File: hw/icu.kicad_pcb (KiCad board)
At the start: 2 copper layers, 60 x 90 mm, 99 parts, among them J1001 ARM_JTAG_SWD_HEADER_10_PINSMD, J101 AMPSEAL_8_POS_VERT_BLACK_SEAL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, J102 AMPSEAL_23_POS_VERT_GRAY_SEAL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, U1001 MCP2551_SOIC8, U1002 LPC1549JBD64, U301 VND5050AJTR-E, U401 VND5050AJTR-E, U501 VND5050AJTR-E, U601 VND5050AJTR-E, U701 VND5050AJTR-E, U801 VND5050AJTR-E, U901 VND5050AJTR-E, X1001 XTAL_7A-12.000MAAJ-T

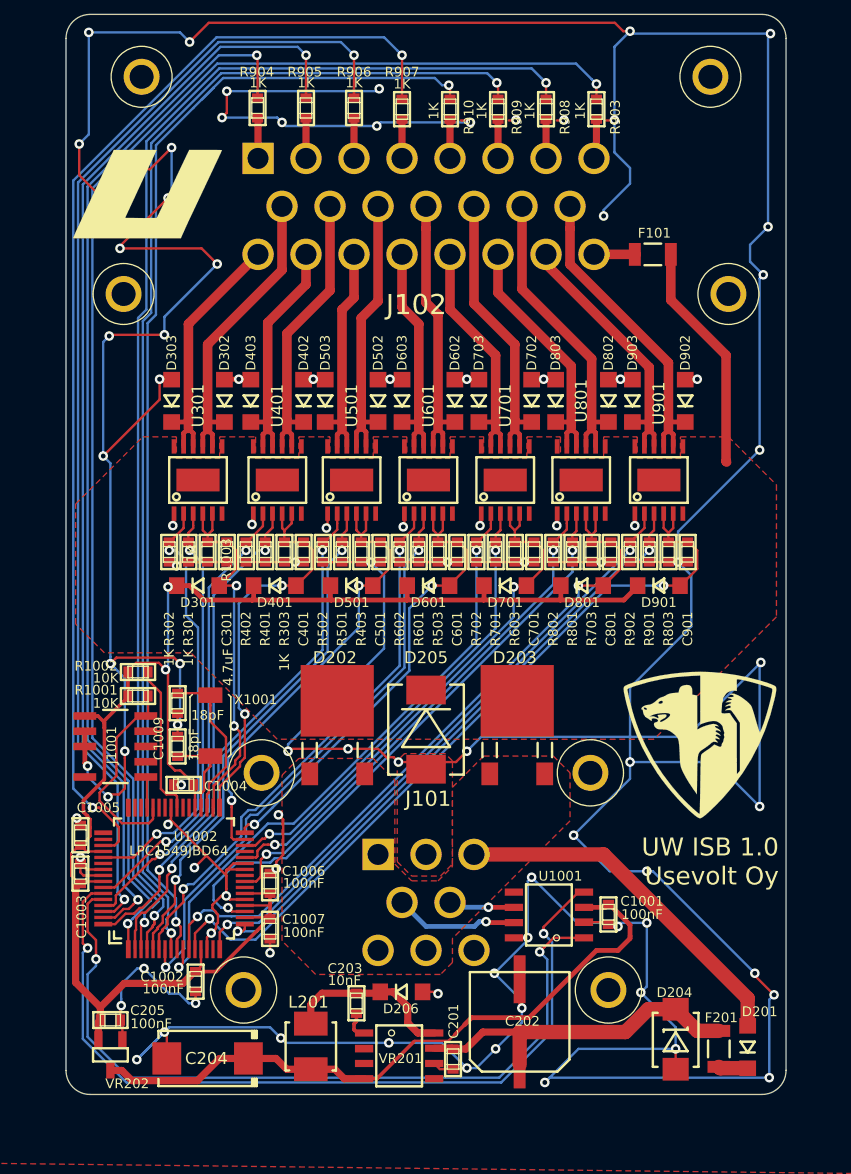
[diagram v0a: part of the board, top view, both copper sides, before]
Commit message: pcb 2.0 created, with imu
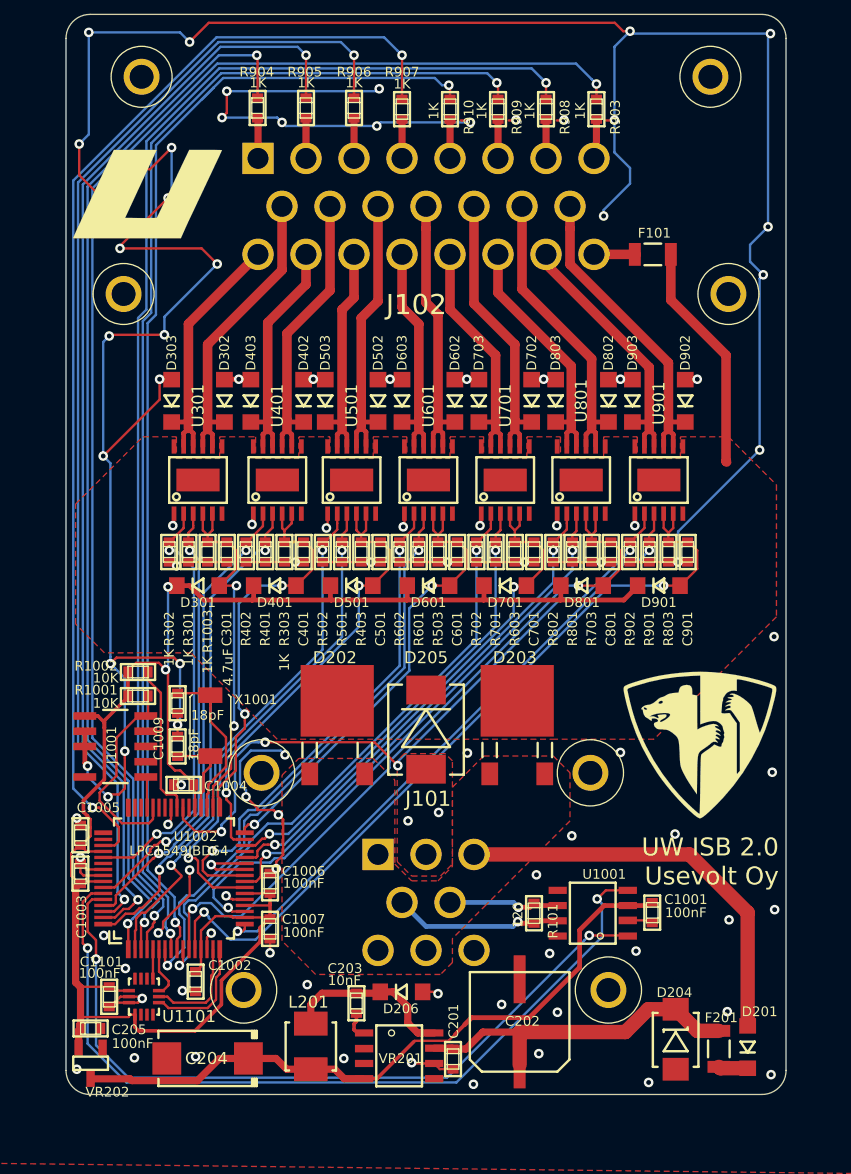
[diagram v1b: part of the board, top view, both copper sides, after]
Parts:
- added C1101: 100nF, kemet:0603, F.Cu at (141.6, 130.9)
- added R101: 120, yageo:0603, F.Cu at (177.0, 123.9)
- added U1101: IMU_LSM6DS3USTR, usevolt:LGA-14, F.Cu at (144.5, 130.9)
- moved C1001 3.65 mm to (186.8, 123.8)
- moved U1001 3.65 mm to (181.9, 123.9)
- moved VR202 1.79 mm to (140.1, 136.4)
- moved C205 1.79 mm to (140.1, 133.5)
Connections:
- net /5V_OUT renamed /VDD_OUT
- U1002 pad P$15: (no net) -> /lpc1549/SCK
- U1002 pad P$16: /Sheet5A7B753C/IN2 -> /Sheet5B43633F/CS
- U1002 pad P$23: (no net) -> /Sheet5A7B341A/IN1
- U1002 pad P$25: (no net) -> /Sheet5A7B3FAC/IN2
- U1002 pad P$39: (no net) -> /Sheet5A7B753C/IN2
- U1002 pad P$5: /Sheet5A7B341A/IN1 -> /Sheet5B43633F/MISO
- U1002 pad P$6: /Sheet5A7B3FAC/IN2 -> /Sheet5B43633F/MOSI
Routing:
- net GND: track 661.3 -> 399.1 mm, vias 96 -> 100
- net +3V3: track 138.6 -> 154.2 mm
- net /Sheet5B43633F/CS: track 0.00 -> 10.2 mm
- net /lpc1549/SCK: track 0.00 -> 8.81 mm
- net /Sheet5B43633F/MOSI: track 0.00 -> 4.32 mm
- net /Sheet5A7B753C/IN2: track 52.4 -> 56.7 mm, vias 2 -> 4
- net /Power supply/VIN: track 30.1 -> 34.2 mm
- net /lpc1549/CANL: track 5.49 -> 9.36 mm
- net /lpc1549/CANH: track 10.3 -> 14.1 mm
- net /Sheet5A7B3FAC/IN2: track 45.7 -> 42.0 mm
- net /Sheet5A7B341A/IN1: track 43.0 -> 40.5 mm
- net /Sheet5B43633F/MISO: track 0.00 -> 2.46 mm
- net /lpc1549/CAN_TX: track 65.4 -> 63.9 mm
- net /lpc1549/OUT7_SENSE: track 65.7 -> 66.8 mm
- net /lpc1549/OUT6_SENSE: track 59.9 -> 60.8 mm
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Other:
- board text added: "UW ISB 2.0 Usevolt Oy"
- board text removed: "UW ISB 1.0 Usevolt Oy"

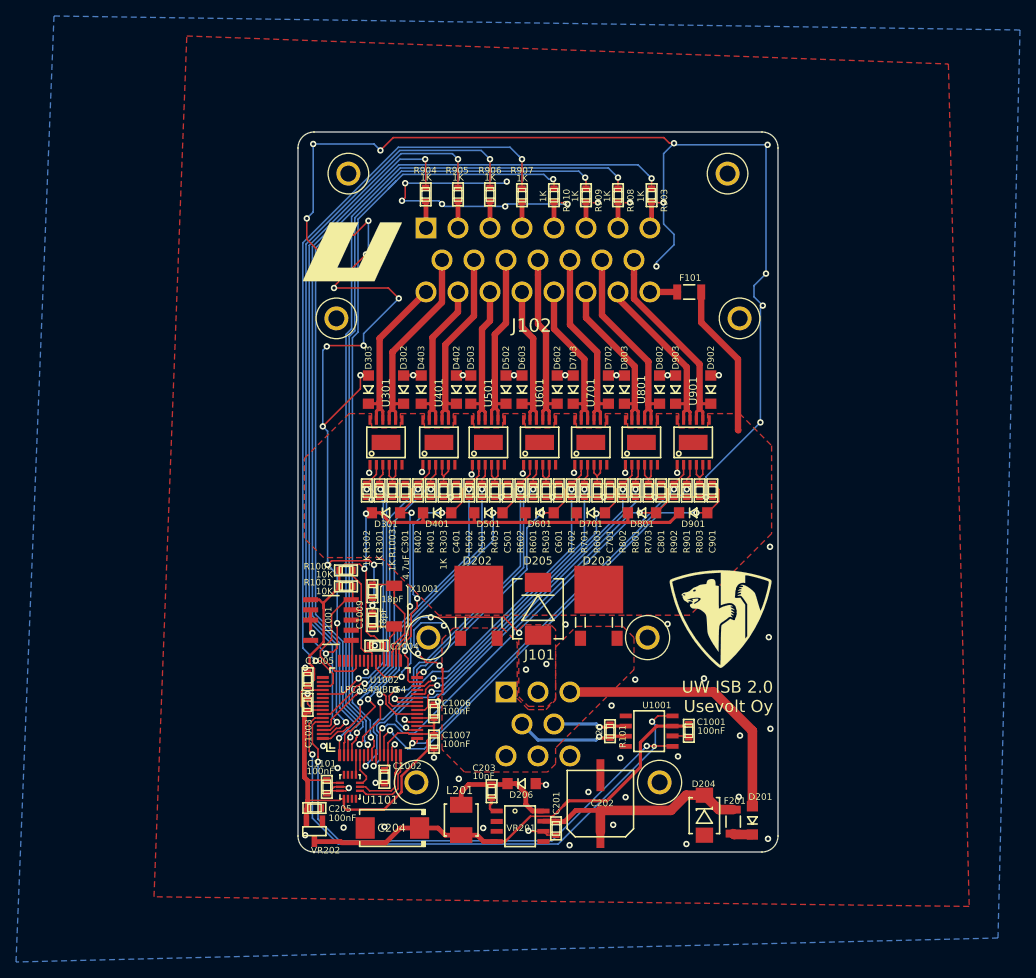
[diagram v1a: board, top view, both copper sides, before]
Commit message: 2 din replaced with ain, zeners added to outputs
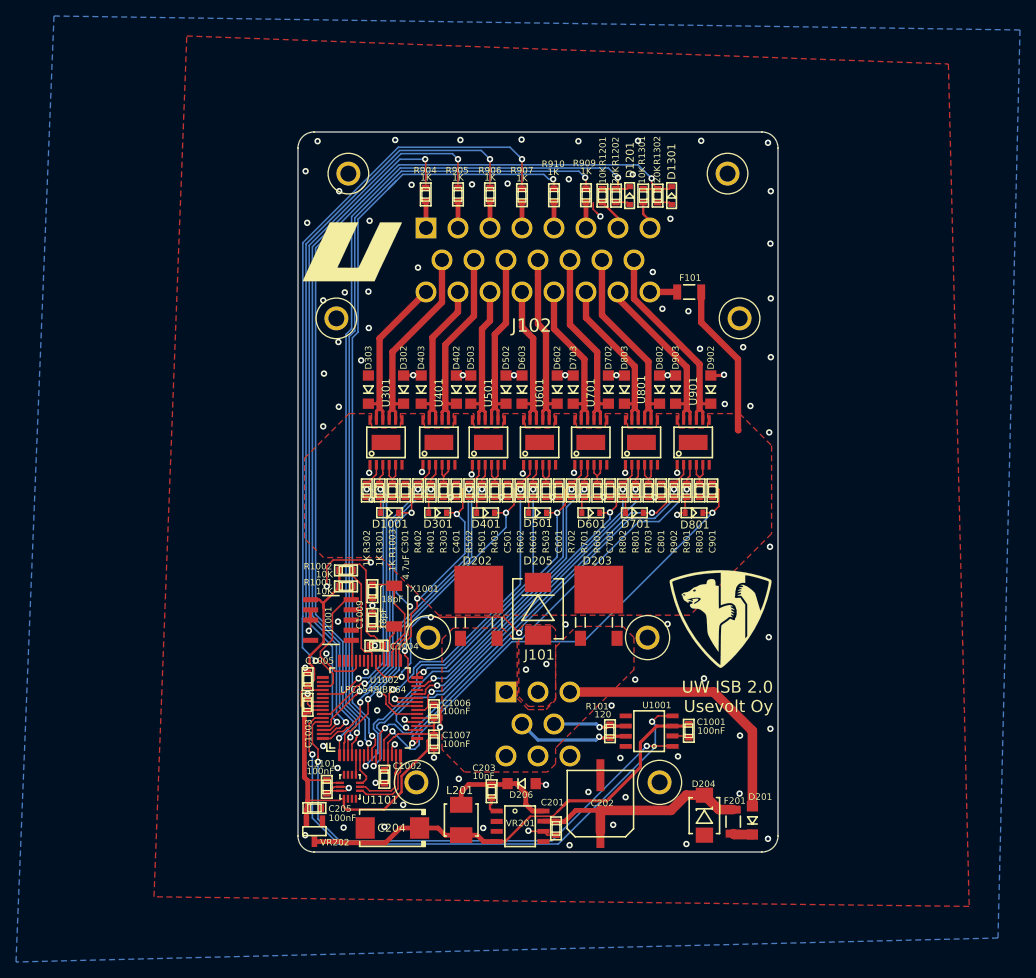
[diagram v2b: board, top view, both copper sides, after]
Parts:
- removed D901: DIODE_RS07J-GS18, usevolt:DO219AB
- removed R903, R908: 1K, yageo:0603
- added D1001: ZENER_MM3Z3V6T1G, usevolt:SOD-323, F.Cu at (149.4, 96.6)
- added D1201: ZENER_MM3Z3V6T1G, usevolt:SOD-323, F.Cu at (179.4, 57.0)
- added D1301: ZENER_MM3Z3V6T1G, usevolt:SOD-323, F.Cu at (184.7, 57.0)
- added R1201: 10K, yageo:0603, F.Cu at (176.1, 57.0)
- added R1202: 20K, yageo:0603, F.Cu at (177.8, 57.0)
- added R1301: 10K, yageo:0603, F.Cu at (181.2, 57.0)
- added R1302: 20K, yageo:0603, F.Cu at (182.9, 57.0)
- D301, D401, D501, D601, D701, D801: value DIODE_RS07J-GS18 -> ZENER_MM3Z3V6T1G; footprint usevolt:DO219AB -> usevolt:SOD-323
- moved D801 6.50 mm to (187.5, 96.6)
- moved D301 6.45 mm to (155.4, 96.6)
- moved D601 6.40 mm to (174.6, 96.6)
- moved D501 6.15 mm to (167.9, 96.6)
- moved D401 6.05 mm to (161.4, 96.6)
- moved D701 5.45 mm to (180.1, 96.6)
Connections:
- J102 pad 7: /lpc1549/DIN7 -> /Sheet5B70DDCA/VIN
- J102 pad 8: /lpc1549/DIN8 -> /Sheet5B73B712/VIN
- U1002 pad P$3: Net-(R903-Pad1) -> /lpc1549/AIN1
- U1002 pad P$4: Net-(R908-Pad1) -> /lpc1549/AIN2
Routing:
- net GND: track 399.1 -> 125.8 mm, vias 100 -> 113
- net /lpc1549/AIN1: track 0.00 -> 118.2 mm, vias 0 -> 2
- net Net-(R903-Pad1): track 114.6 -> 0.00 mm, vias 2 -> 0
- net /lpc1549/AIN2: track 0.00 -> 110.0 mm, vias 0 -> 2
- net Net-(R908-Pad1): track 106.7 -> 0.00 mm, vias 2 -> 0
- net +3V3: track 154.2 -> 100.8 mm, vias 2 -> 0
- net /Sheet5B70DDCA/VIN: track 0.00 -> 3.94 mm
- net /Sheet5B73B712/VIN: track 0.00 -> 3.84 mm
- net /lpc1549/DIN8: track 3.63 -> 0.00 mm
- net /lpc1549/DIN7: track 3.26 -> 0.00 mm
- net /lpc1549/OUT7_SENSE: track 66.8 -> 68.8 mm
- net /lpc1549/OUT4_SENSE: track 39.7 -> 41.3 mm
- net /Sheet5A7B3FAC/IN1: track 49.0 -> 50.4 mm
- net /lpc1549/OUT1_SENSE: track 31.5 -> 32.8 mm
- net /Sheet5A7B753C/IN1: track 51.8 -> 52.6 mm
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
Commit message: CM_6.2.1 delivered, first customer machine with CCU, HCU & ICU
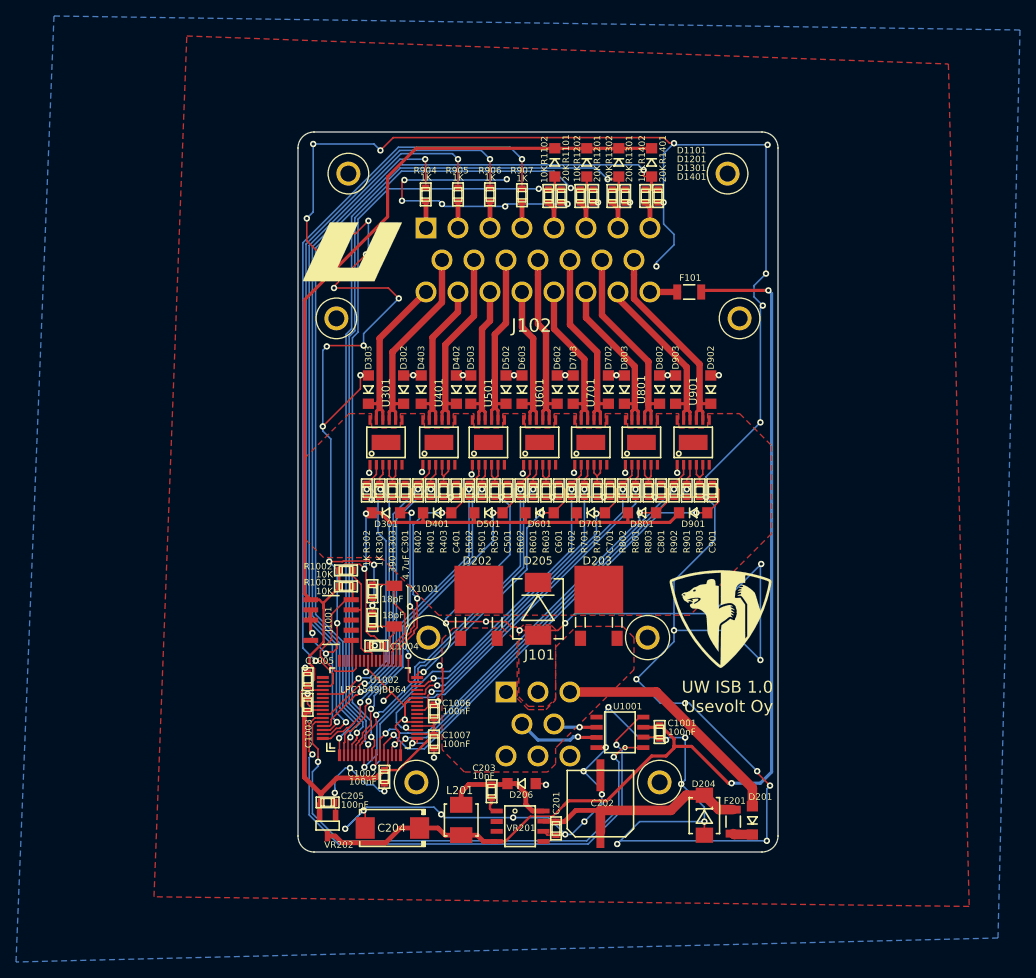
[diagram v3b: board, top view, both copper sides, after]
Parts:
- removed C1009: 18pF, kemet:0603
- removed C1101: 100nF, kemet:0603
- removed D1001: ZENER_MM3Z3V6T1G, usevolt:SOD-323
- removed R1003, R909, R910: 1K, yageo:0603
- removed R101: 120, yageo:0603
- removed U1101: IMU_LSM6DS3USTR, usevolt:LGA-14
- added D1101: DIODE_RS07J-GS18, usevolt:DO219AB, F.Cu at (170.1, 52.8)
- added D1401: DIODE_RS07J-GS18, usevolt:DO219AB, F.Cu at (182.2, 52.8)
- added D901: DIODE_RS07J-GS18, usevolt:DO219AB, F.Cu at (187.4, 96.6)
- added R1101: 10K, yageo:0603, F.Cu at (169.3, 57.0)
- added R1102: 20K, yageo:0603, F.Cu at (170.9, 57.0)
- added R1401: 10K, yageo:0603, F.Cu at (181.4, 57.0)
- added R1402: 20K, yageo:0603, F.Cu at (183.0, 57.0)
- added R903: 390, yageo:0603, F.Cu at (188.2, 93.8)
- added eC1009: 18pF, kemet:0603, F.Cu at (147.3, 110.0)
- D1201, D1301, D301, D401, D501, D601, D701, D801: value ZENER_MM3Z3V6T1G -> DIODE_RS07J-GS18; footprint usevolt:SOD-323 -> usevolt:DO219AB
- R303, R403, R503, R603, R703, R803: value 1K -> 390
- moved D1301 7.80 mm to (178.1, 52.8), turned to 90 degrees
- moved D1201 6.77 mm to (174.1, 52.8), turned to 90 degrees
- moved D801 6.50 mm to (181.0, 96.6)
- moved D301 6.45 mm to (149.0, 96.6)
- moved D601 6.40 mm to (168.2, 96.6)
- moved R403 6.40 mm to (156.2, 93.8)
- moved R503 6.40 mm to (162.6, 93.8)
- moved R603 6.40 mm to (169.0, 93.8)
- moved R703 6.40 mm to (175.4, 93.8)
- moved R303 6.40 mm to (149.8, 93.8)
- moved R803 6.40 mm to (181.8, 93.8)
- moved D501 6.15 mm to (161.8, 96.6)
- moved D401 6.05 mm to (155.4, 96.6)
- moved D701 5.45 mm to (174.6, 96.6)
- moved R1302 4.05 mm to (178.9, 57.0)
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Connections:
- net /VDD_OUT renamed /5V_OUT
- F101 pad P$1: VDD -> +5V
- J102 pad 5: /lpc1549/DIN5 -> /Sheet5A7E031D/VIN
- J102 pad 6: /lpc1549/DIN6 -> /Sheet5A7E2A6D/VIN
- J102 pad 7: /Sheet5B70DDCA/VIN -> /Sheet5A7E34B9/VIN
- J102 pad 8: /Sheet5B73B712/VIN -> /Sheet5A8C5347/VIN
- R1201 pad 2: /Sheet5B70DDCA/VIN -> /Sheet5A7E2A6D/VIN
- R1301 pad 1: /lpc1549/AIN1 -> /lpc1549/AIN3
- R1301 pad 2: /Sheet5B73B712/VIN -> /Sheet5A7E34B9/VIN
- R1302 pad 2: /lpc1549/AIN1 -> /lpc1549/AIN3
- R303 pad 1: /lpc1549/OUT2_SENSE -> /lpc1549/OUT1_SENSE
- R403 pad 1: /lpc1549/OUT3_SENSE -> /lpc1549/OUT2_SENSE
- R503 pad 1: /lpc1549/OUT4_SENSE -> /lpc1549/OUT3_SENSE
- R603 pad 1: /lpc1549/OUT5_SENSE -> /lpc1549/OUT4_SENSE
- R703 pad 1: /lpc1549/OUT6_SENSE -> /lpc1549/OUT5_SENSE
- R803 pad 1: /lpc1549/OUT7_SENSE -> /lpc1549/OUT6_SENSE
- U1002 pad P$15: /lpc1549/SCK -> (no net)
- U1002 pad P$16: /Sheet5B43633F/CS -> /Sheet5A7B753C/IN2
- U1002 pad P$23: /Sheet5A7B341A/IN1 -> (no net)
- U1002 pad P$25: /Sheet5A7B3FAC/IN2 -> (no net)
- U1002 pad P$3: /lpc1549/AIN1 -> /lpc1549/AIN4
- U1002 pad P$39: /Sheet5A7B753C/IN2 -> (no net)
- U1002 pad P$4: /lpc1549/AIN2 -> /lpc1549/AIN3
- U1002 pad P$5: /Sheet5B43633F/MISO -> /Sheet5A7B341A/IN1
- U1002 pad P$6: /Sheet5B43633F/MOSI -> /Sheet5A7B3FAC/IN2
- U1002 pad P$8: Net-(R909-Pad1) -> /lpc1549/AIN2
- U1002 pad P$9: Net-(R910-Pad1) -> /lpc1549/AIN1
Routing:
- net GND: track 125.8 -> 658.2 mm, vias 113 -> 96
- net +3V3: track 100.8 -> 230.6 mm, vias 0 -> 2
- net /lpc1549/AIN4: track 0.00 -> 117.1 mm, vias 0 -> 2
- net /lpc1549/AIN3: track 0.00 -> 108.9 mm, vias 0 -> 2
- net Net-(R909-Pad1): track 101.5 -> 0.00 mm, vias 2 -> 0
- net Net-(R910-Pad1): track 98.2 -> 0.00 mm, vias 2 -> 0
- net +5V: track 56.3 -> 139.3 mm, vias 0 -> 2
- net /lpc1549/AIN1: track 118.2 -> 97.2 mm
- net VDD: track 19.2 -> 0.00 mm
- net /Sheet5B43633F/CS: track 10.2 -> 0.00 mm
- net /lpc1549/SCK: track 8.81 -> 0.00 mm
- net /lpc1549/AIN2: track 110.0 -> 103.3 mm
- net /Sheet5A7B753C/IN2: track 57.4 -> 52.4 mm, vias 4 -> 2
- net /Sheet5B43633F/MOSI: track 4.32 -> 0.00 mm
- net /Power supply/VIN: track 34.2 -> 30.1 mm
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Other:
- board text added: "UW ISB 1.0 Usevolt Oy"
- board text removed: "UW ISB 2.0 Usevolt Oy"
